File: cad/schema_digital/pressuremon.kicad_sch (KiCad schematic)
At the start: 12 parts, among them J1 Digital Pressure 1, J2 Digital Pressure 2, Q1 BC337, U3 DS18B20

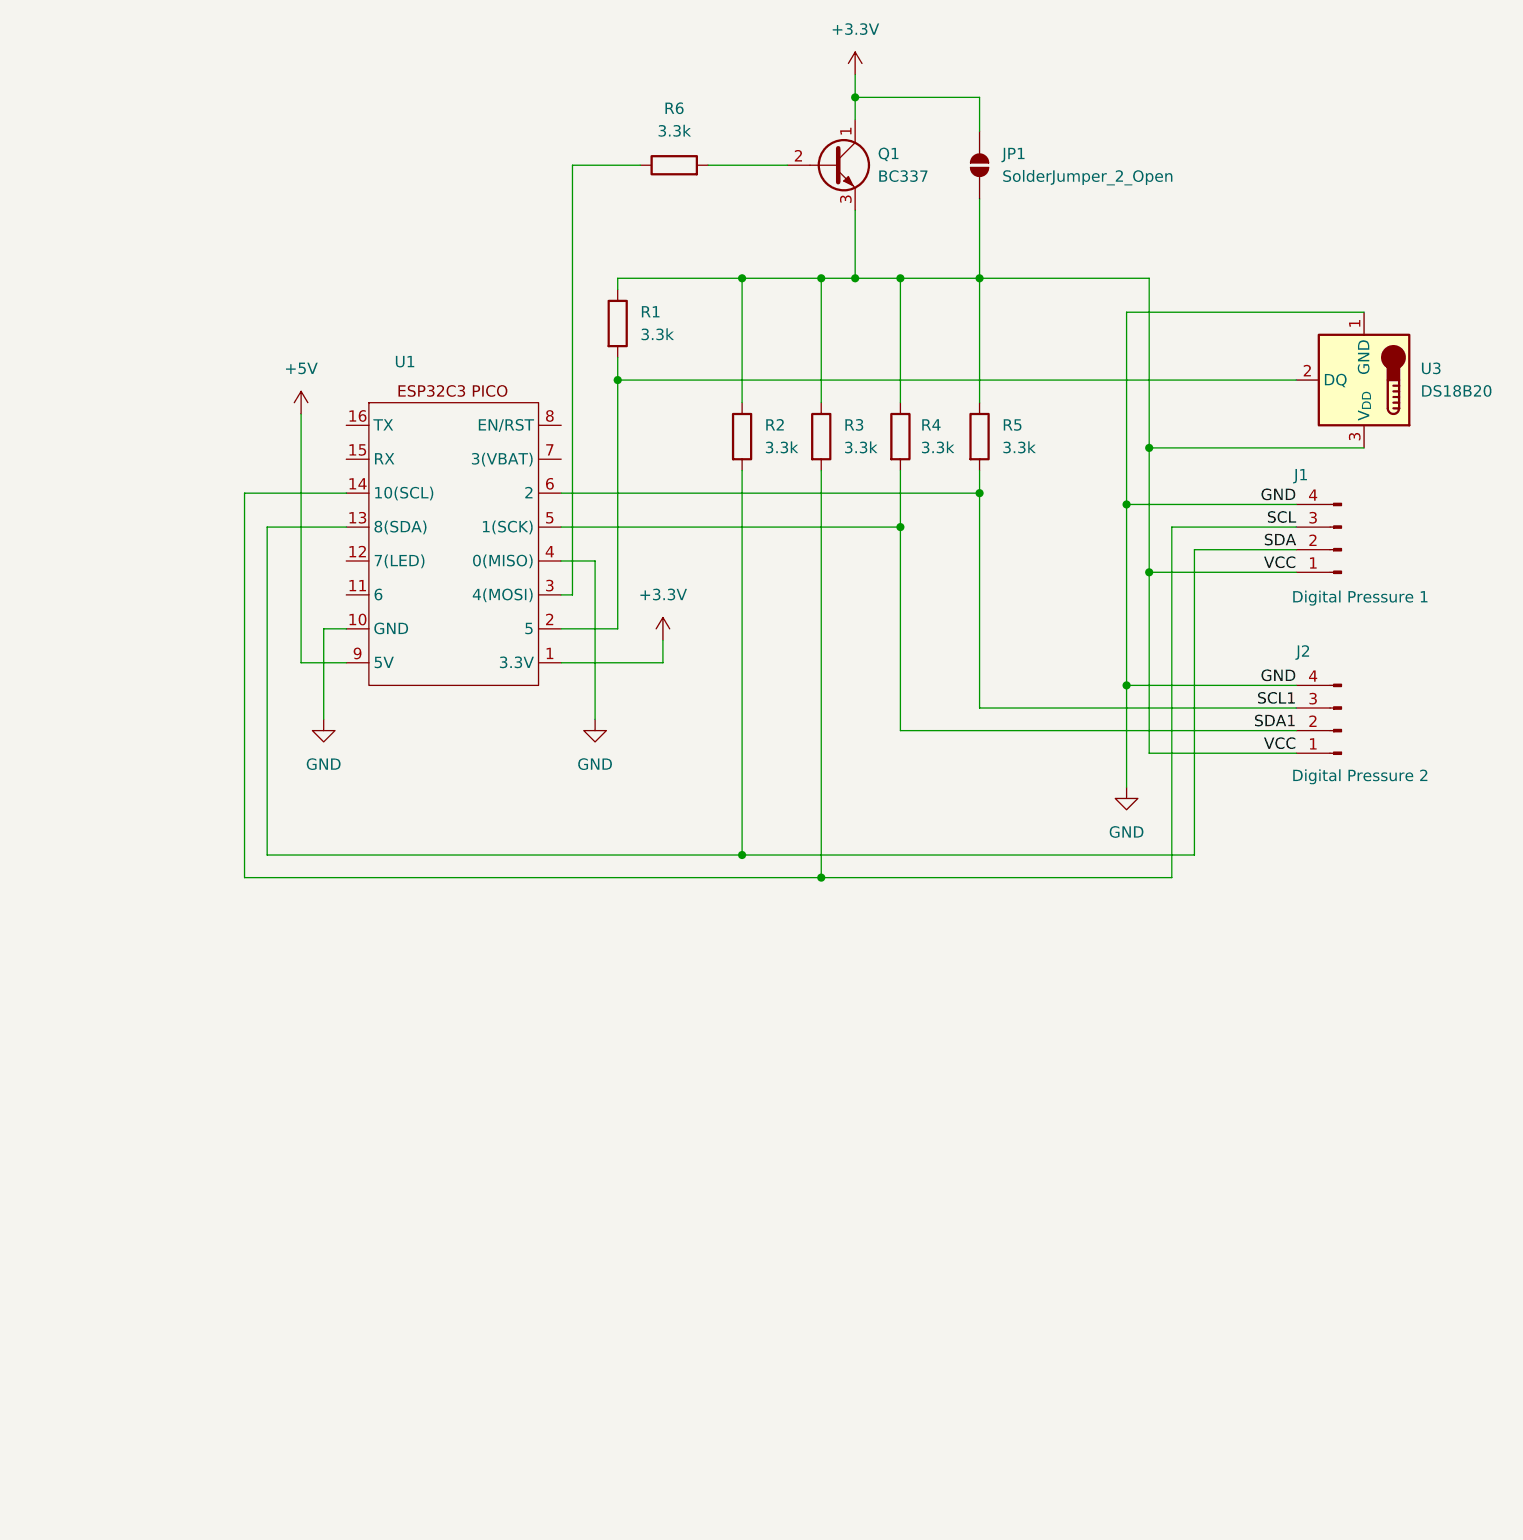
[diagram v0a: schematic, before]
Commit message: Update pcb for digital sensors
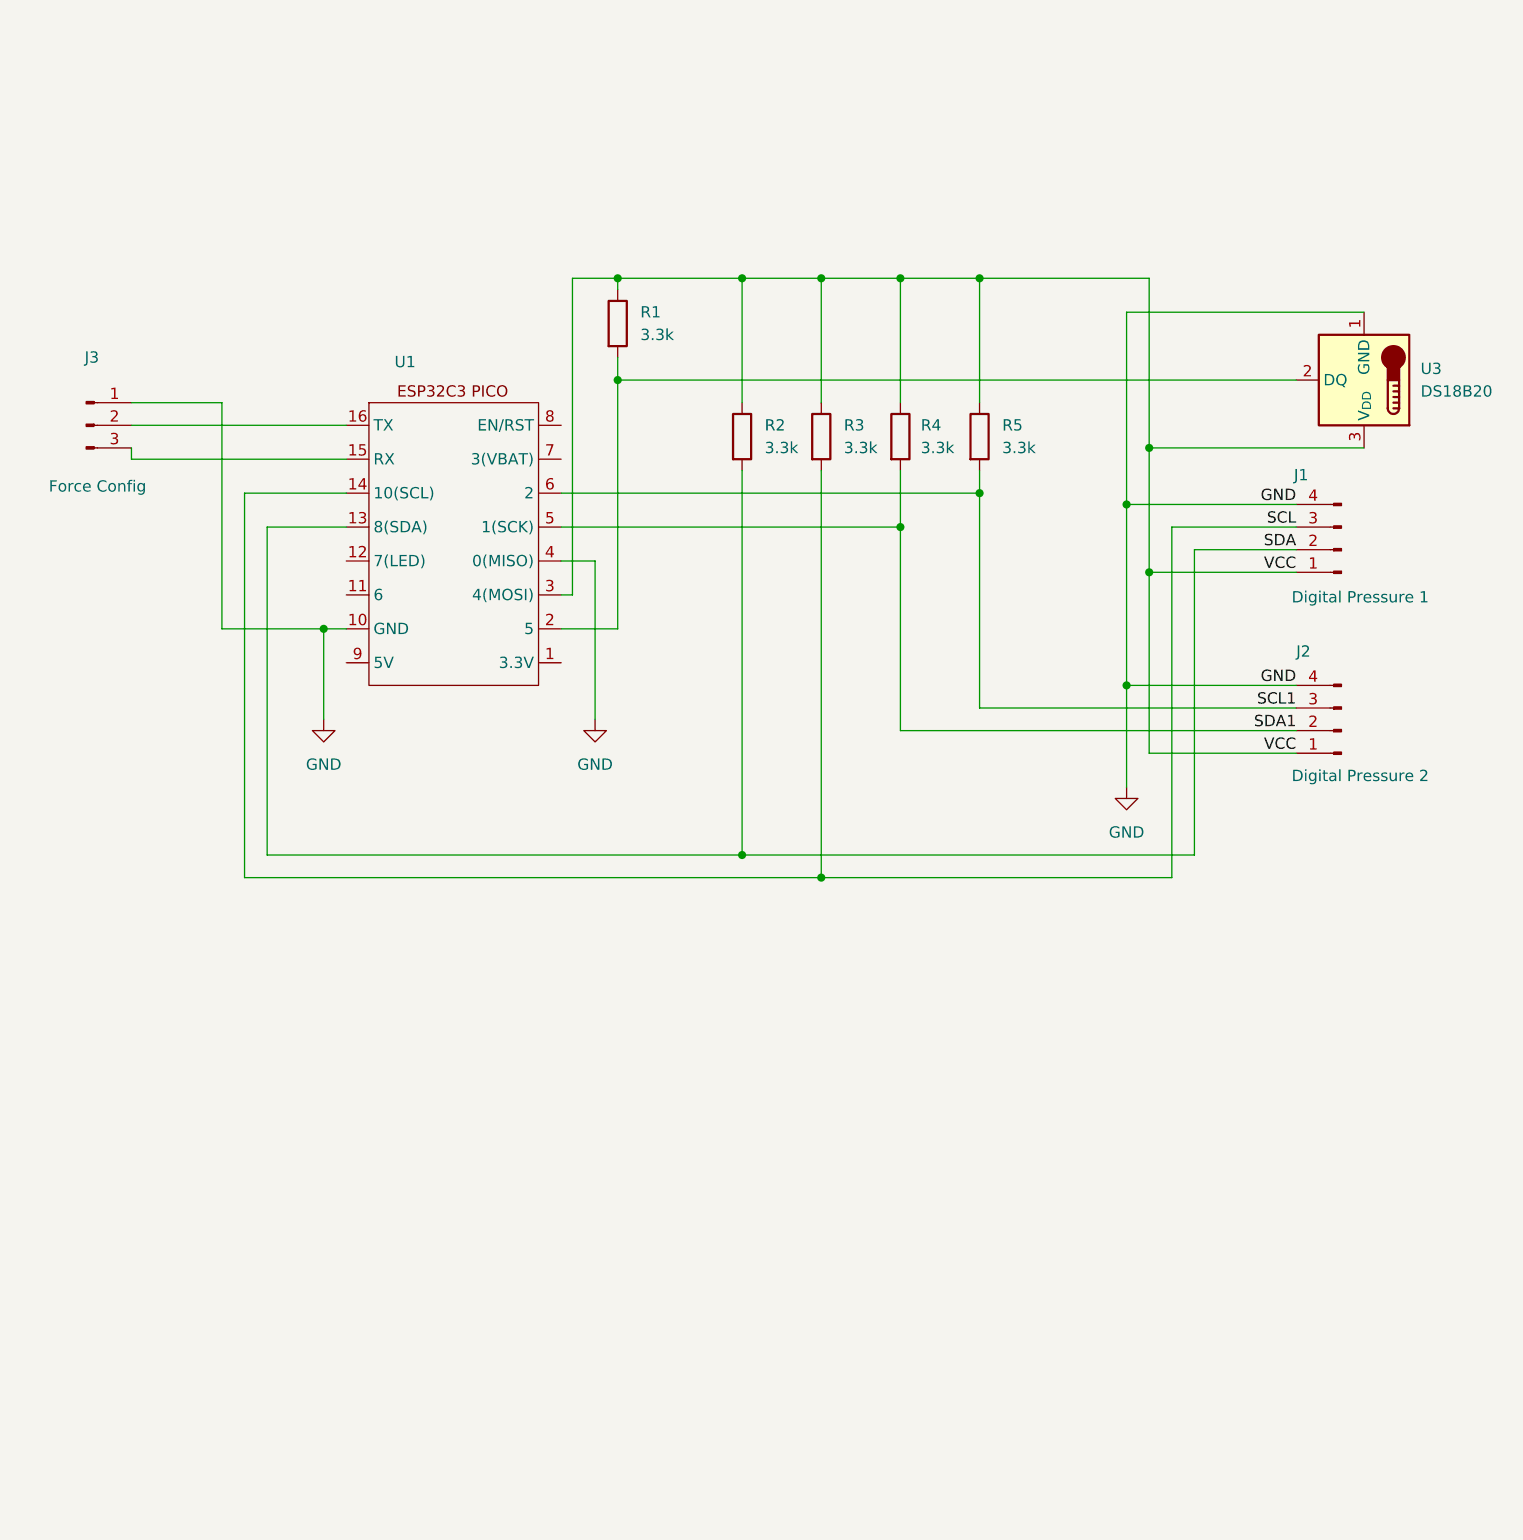
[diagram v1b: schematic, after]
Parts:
- removed JP1: SolderJumper_2_Open, Jumper:SolderJumper-2_P1.3mm_Open_RoundedPad1.0x1.5mm, symbol Jumper:SolderJumper_2_Open
- removed Q1: BC337, Package_TO_SOT_THT:TO-92_Inline_Wide, symbol Transistor_BJT:BC337
- removed R6: 3.3k, Resistor_THT:R_Axial_DIN0204_L3.6mm_D1.6mm_P7.62mm_Horizontal, symbol Device:R
- added J3: Force Config, Connector_PinHeader_2.54mm:PinHeader_1x03_P2.54mm_Vertical, symbol Connector:Conn_01x03_Pin
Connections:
- net GND: now also J3.1 (Pin_1)
- net VCC: now also U1.3 (4(MOSI))
- net at U1.15 (RX): now also J3.3 (Pin_3)
- net at U1.16 (TX): now also J3.2 (Pin_2)
- net +3.3V: no longer names the net of U1.1 (3.3V)
- net +5V: no longer names the net of U1.9 (5V)

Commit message: Update pcb to v1.2
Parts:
- removed U1: ~, pressuremon_library:ESP32C3-pico, symbol myCommonSymbols:ESP32C3-pico
- added U1: ~, pressuremon_library:ESP32C3-pico, symbol pressuremon_library:ESP32C3-pico
- J1: value Digital Pressure 1 -> Conn_01x04_Pin
- J2: value Digital Pressure 2 -> Conn_01x04_Pin
- J3: value Force Config -> Conn_01x03_Pin
- R1, R2, R3, R4, R5: value 3.3k -> R
- U3: footprint Package_TO_SOT_THT:TO-92_Inline_Wide -> Package_TO_SOT_THT:TO-92_Inline
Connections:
- net GND: now also U1.15 (GND), U1.4 (0(MISO))
- net SCL: now also U1.11 (10(SCL))
- net SCL1: now also U1.6 (2)
- net SDA: now also U1.12 (8(SDA))
- net SDA1: now also U1.5 (1(SCK))
- net VCC: now also U1.3 (4(MOSI))
- net at R1.2, U3.2 (DQ): now also U1.2 (5)
- net at J3.3 (Pin_3): now also U1.10 (RX)
- net at J3.2 (Pin_2): now also U1.9 (TX)
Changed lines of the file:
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@@
 		(dnp no)
 		(fields_autoplaced yes)
-		(property "Reference" "#PWR05"
+		(property "Reference" "#PWR5"
 			(at 81.28 105.41 0)
 			(effects
@@
 			(project "pressuremon"
 				(path "/42dbddbd-b9bd-46e0-88a7-2826e12ac31d"
-					(reference "#PWR05")
+					(reference "#PWR5")
 					(unit 1)
 				)
@@
 			)
 		)
-		(property "Footprint" "Package_TO_SOT_THT:TO-92_Inline_Wide"
+		(property "Footprint" "Package_TO_SOT_THT:TO-92_Inline"
 			(at 193.04 54.61 0)
 			(effects
@@
 			)
 		)
-		(property "Value" "3.3k"
+		(property "Value" "R"
 			(at 127 68.5799 0)
 			(effects
@@
 			)
 		)
-		(property "Value" "3.3k"
+		(property "Value" "R"
 			(at 100.33 68.5799 0)
 			(effects
@@
 			)
 		)
-		(property "Value" "3.3k"
+		(property "Value" "R"
 			(at 109.22 68.5799 0)
 			(effects
@@
 			)
 		)
-		(property "Value" "Digital Pressure 2"
+		(property "Value" "Conn_01x04_Pin"
 			(at 159.512 105.41 0)
 			(effects
@@
 	)
 	(symbol
-		(lib_id "myCommonSymbols:ESP32C3-pico")
+		(lib_id "pressuremon_library:ESP32C3-pico")
 		(at 59.69 80.01 0)
 		(unit 1)
@@
 		(on_board yes)
 		(dnp no)
+		(fields_autoplaced yes)
 		(property "Reference" "U1"
-			(at 59.944 58.928 0)
+			(at 65.405 57.15 0)
 			(effects
 				(font
@@
 			)
 		)
-		(pin "1"
+		(pin "9"
+		)
+		(pin "14"
+		)
+		(pin "15"
+		)
+		(pin "16"
+		)
+		(pin "11"
+		)
+		(pin "12"
 		)
 		(pin "10"
 		)
-		(pin "16"
+		(pin "13"
+		)
+		(pin "8"
 		)
 		(pin "7"
 		)
-		(pin "12"
+		(pin "6"
+		)
+		(pin "5"
+		)
+		(pin "4"
 		)
 		(pin "3"
 		)
-		(pin "6"
-		)
-		(pin "11"
-		)
-		(pin "5"
-		)
-		(pin "14"
-		)
 		(pin "2"
 		)
-		(pin "4"
-		)
-		(pin "13"
-		)
-		(pin "15"
-		)
-		(pin "8"
-		)
-		(pin "9"
+		(pin "1"
 		)
 		(instances
@@
 			)
 		)
-		(property "Value" "Digital Pressure 1"
+		(property "Value" "Conn_01x04_Pin"
 			(at 159.512 85.344 0)
 			(effects
@@
 			)
 		)
-		(property "Value" "3.3k"
+		(property "Value" "R"
 			(at 117.856 68.58 0)
 			(effects
@@
 		(dnp no)
 		(fields_autoplaced yes)
-		(property "Reference" "#PWR01"
+		(property "Reference" "#PWR1"
 			(at 140.97 113.03 0)
 			(effects
@@
 			(project ""
 				(path "/42dbddbd-b9bd-46e0-88a7-2826e12ac31d"
-					(reference "#PWR01")
+					(reference "#PWR1")
 					(unit 1)
 				)
@@
 			)
 		)
-		(property "Value" "3.3k"
+		(property "Value" "R"
 			(at 86.36 55.8799 0)
 			(effects
@@
 		(dnp no)
 		(fields_autoplaced yes)
-		(property "Reference" "#PWR02"
+		(property "Reference" "#PWR2"
 			(at 50.8 105.41 0)
 			(effects
@@
 			(project ""
 				(path "/42dbddbd-b9bd-46e0-88a7-2826e12ac31d"
-					(reference "#PWR02")
+					(reference "#PWR2")
 					(unit 1)
 				)
@@
 			)
 		)
-		(property "Value" "Force Config"
+		(property "Value" "Conn_01x03_Pin"
 			(at 25.4 72.898 0)
 			(effects
